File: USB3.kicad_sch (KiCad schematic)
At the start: 25 parts, among them U10 TPD4EUSB30, U4 TPD4EUSB30, U5 TPD4EUSB30, U6 TUSB7340, U7 TPD4EUSB30, U8 TPD4EUSB30, U9 TPD4EUSB30, Y3 Crystal_Small

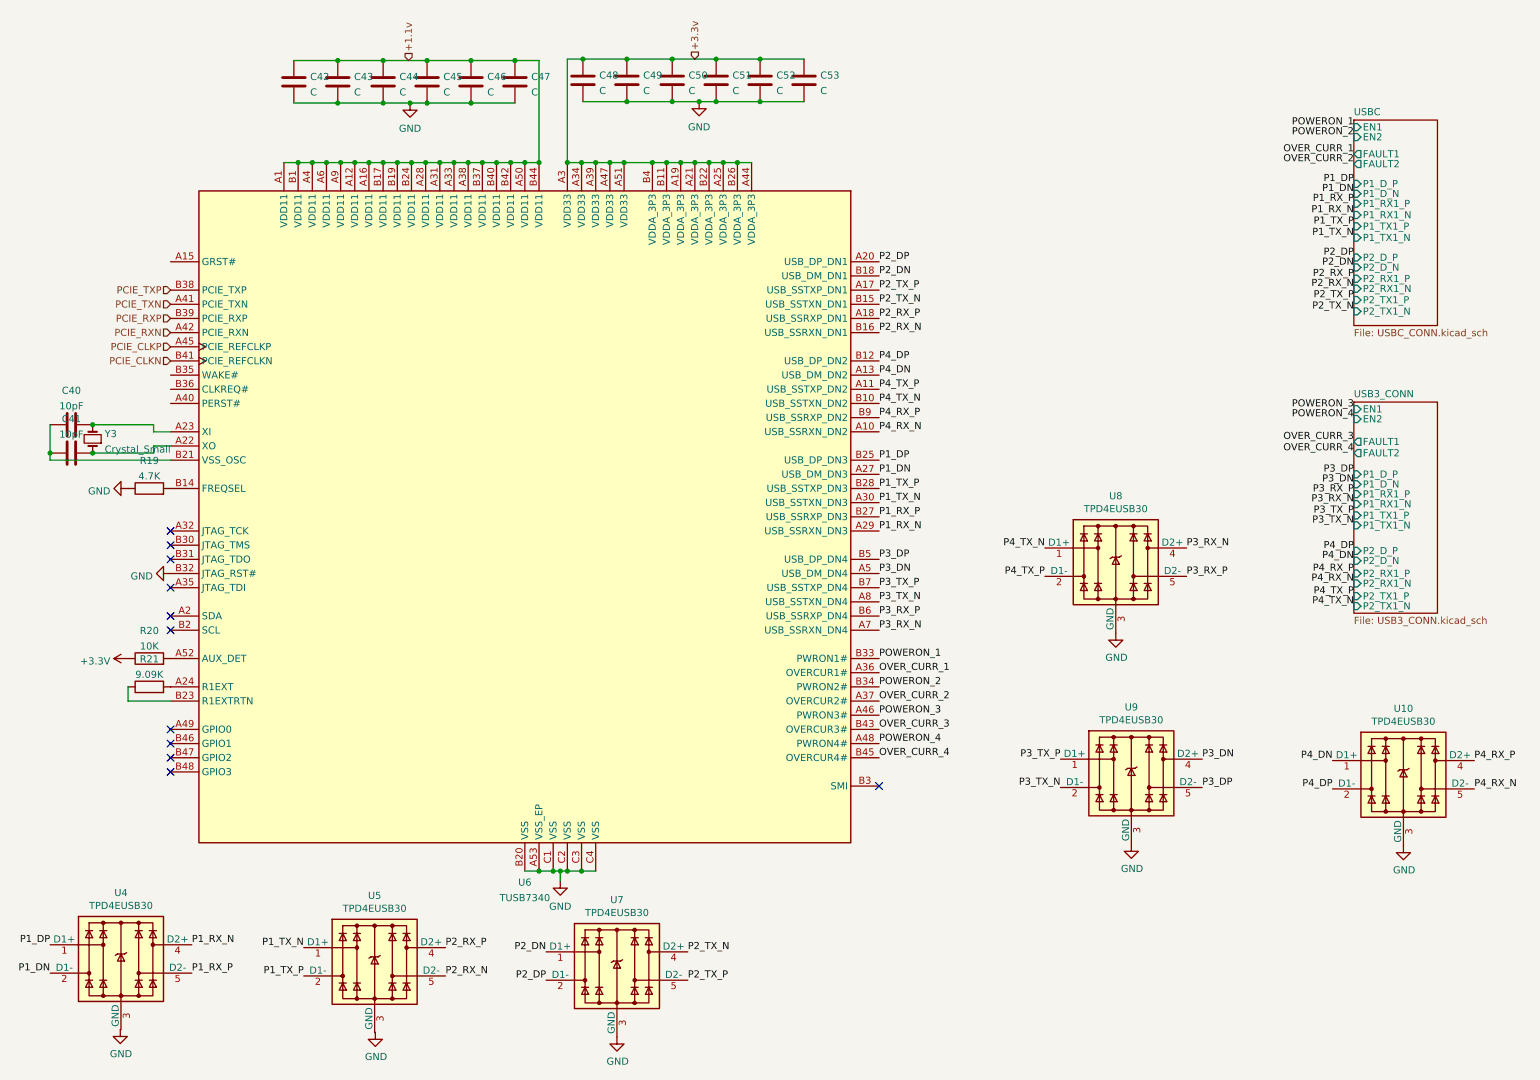
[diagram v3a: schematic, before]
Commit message: Added usb to ethernet and changed mcu to stm32g4
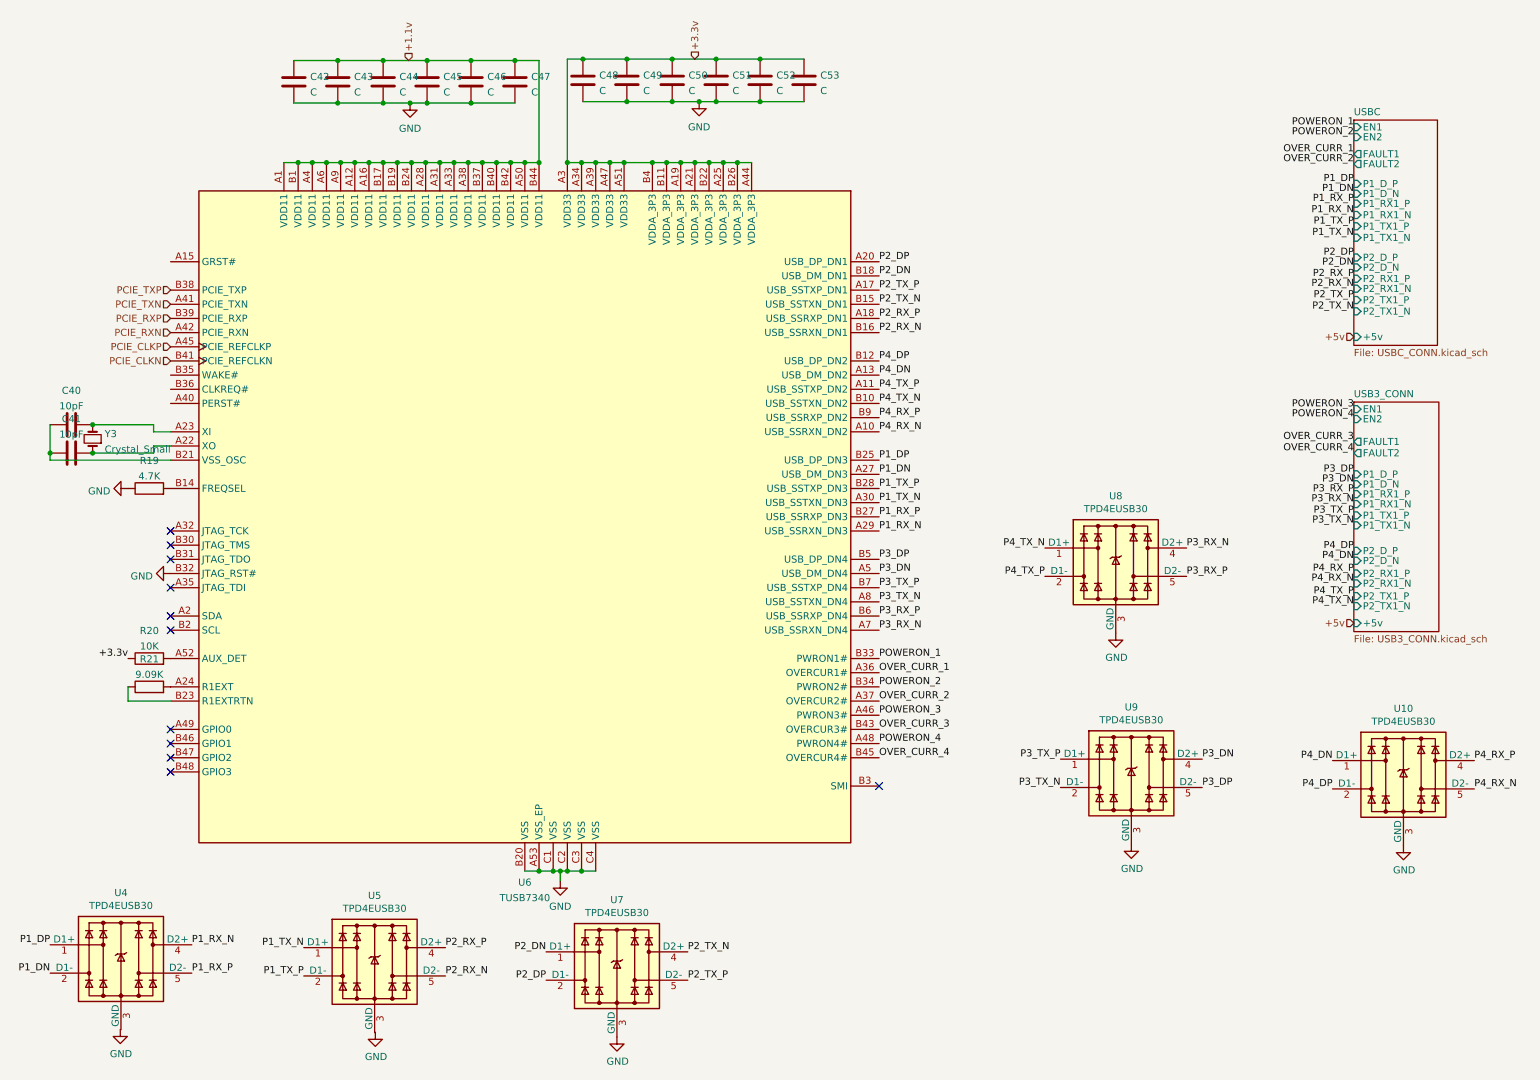
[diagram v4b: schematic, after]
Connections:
- net +3V3 is gone; now on net +3.3v: R20.1
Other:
- sheet USB3_CONN ports: added +5v; removed none
- sheet USBC ports: added +5v; removed none
